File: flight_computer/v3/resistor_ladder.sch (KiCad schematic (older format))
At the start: 58 parts, among them U18 ADG841YKSZ-500RL7, U19 ADG841YKSZ-500RL7, U20 ADG841YKSZ-500RL7, U21 CD4516B_PW_16, U22 ADG841YKSZ-500RL7, U26 CD4516B_PW_16, U28 ADG841YKSZ-500RL7, U29 ADG841YKSZ-500RL7, U30 ADG841YKSZ-500RL7, U31 CD4516B_PW_16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

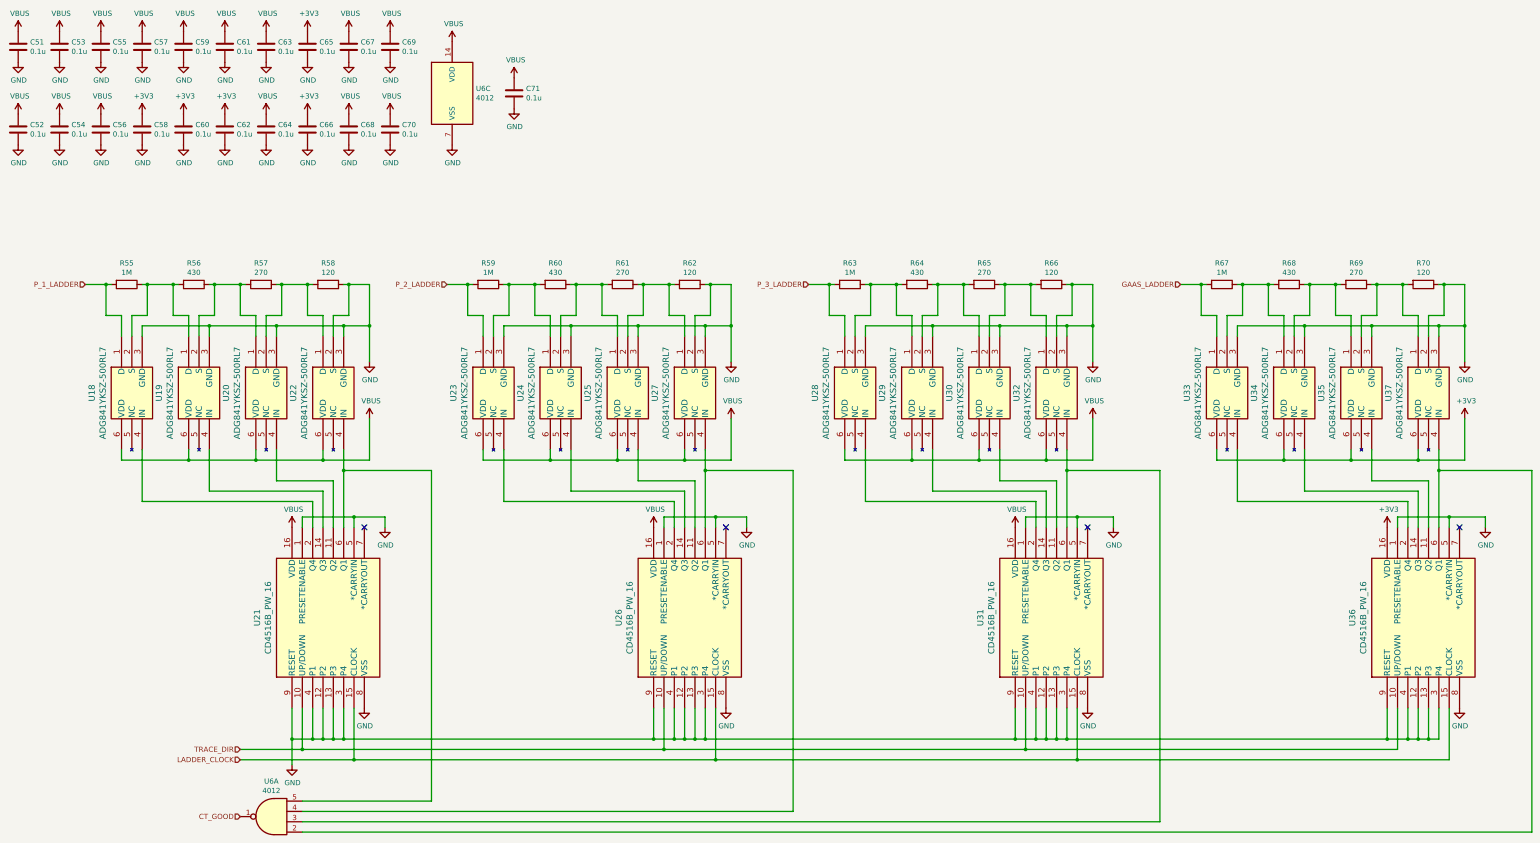
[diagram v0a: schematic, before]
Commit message: Update hardware
- Add separate discharge resistance paths to flight computer
- Update footprint for payload holder
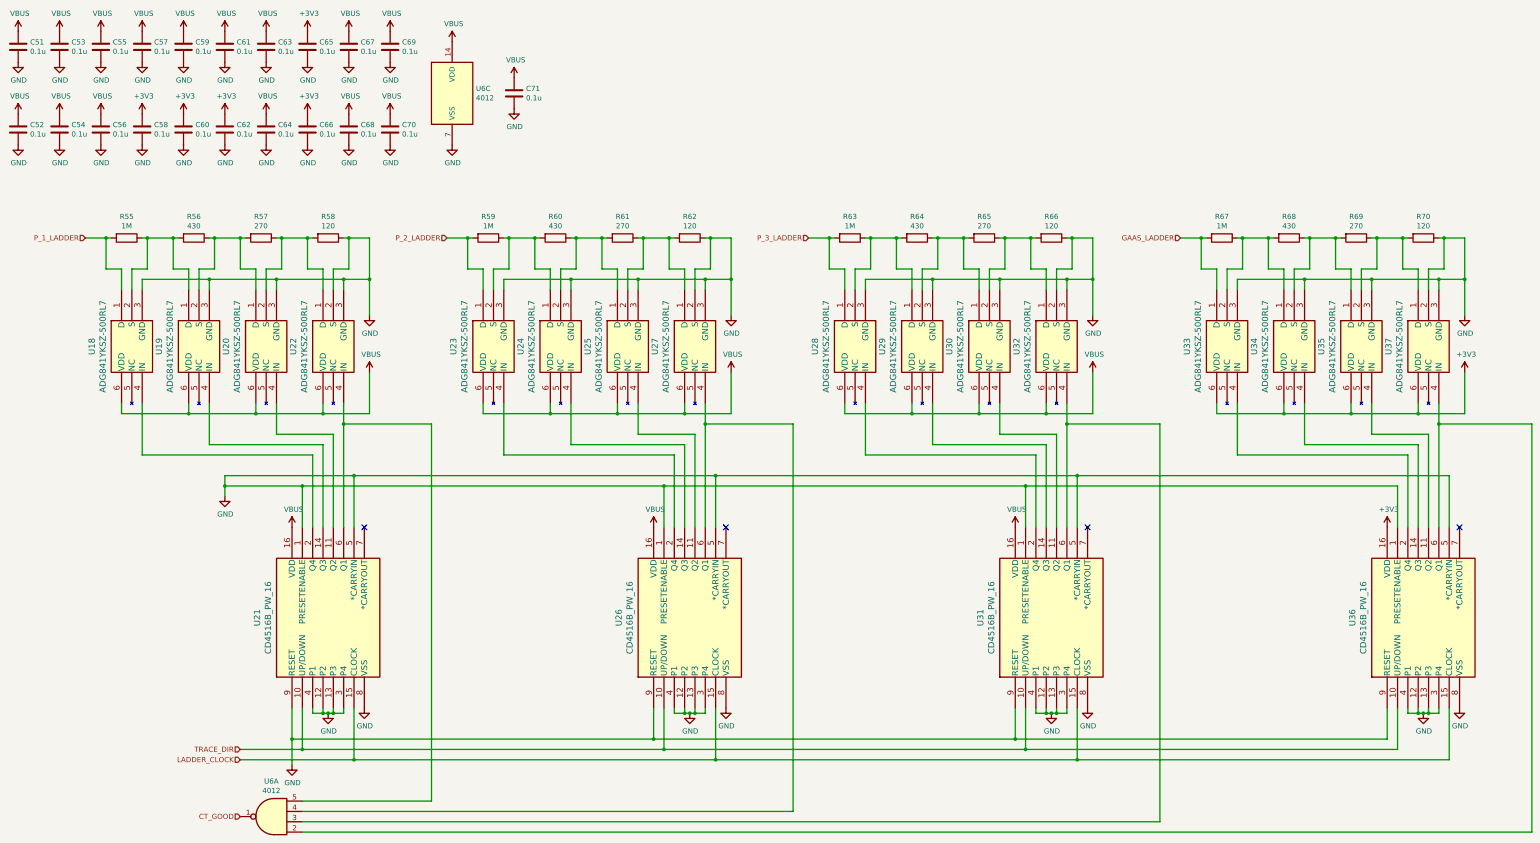
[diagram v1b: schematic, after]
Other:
- moved on the sheet: R55, R56, R57, R58, R59, R60, R61, R62, R63, R64, R65, R66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
